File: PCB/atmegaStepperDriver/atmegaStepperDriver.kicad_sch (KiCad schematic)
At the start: 74 parts, among them J1 General power, J2 Motor Output, J3 Motor power, J4 Conn_01x05_Socket, J5 Reset Header, J6 I2C Communication pins, J9 Stepper communication pins, Q1 TIP42C, Q10 BC547, Q11 BC557, Q12 BC547, Q13 BC557, Q14 BC547, Q15 BC557, Q16 BC547, Q2 TIP41C, Q3 TIP42C, Q4 TIP42C, Q5 TIP42C, Q6 TIP41C, Q7 TIP41C, Q8 TIP41C, Q9 BC557, U1 ATmega328P-P, U2 LM7805_TO220, Y1 Crystal

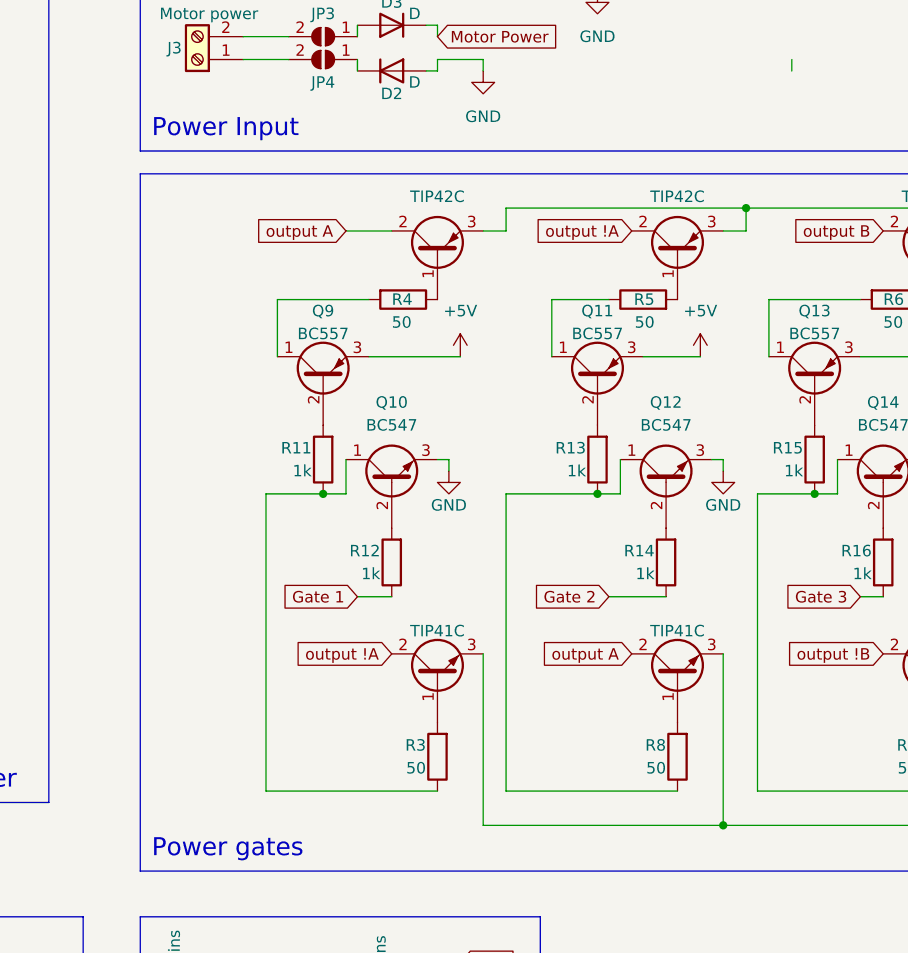
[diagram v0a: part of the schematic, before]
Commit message: new design; the old one doesn't work; to be finished;
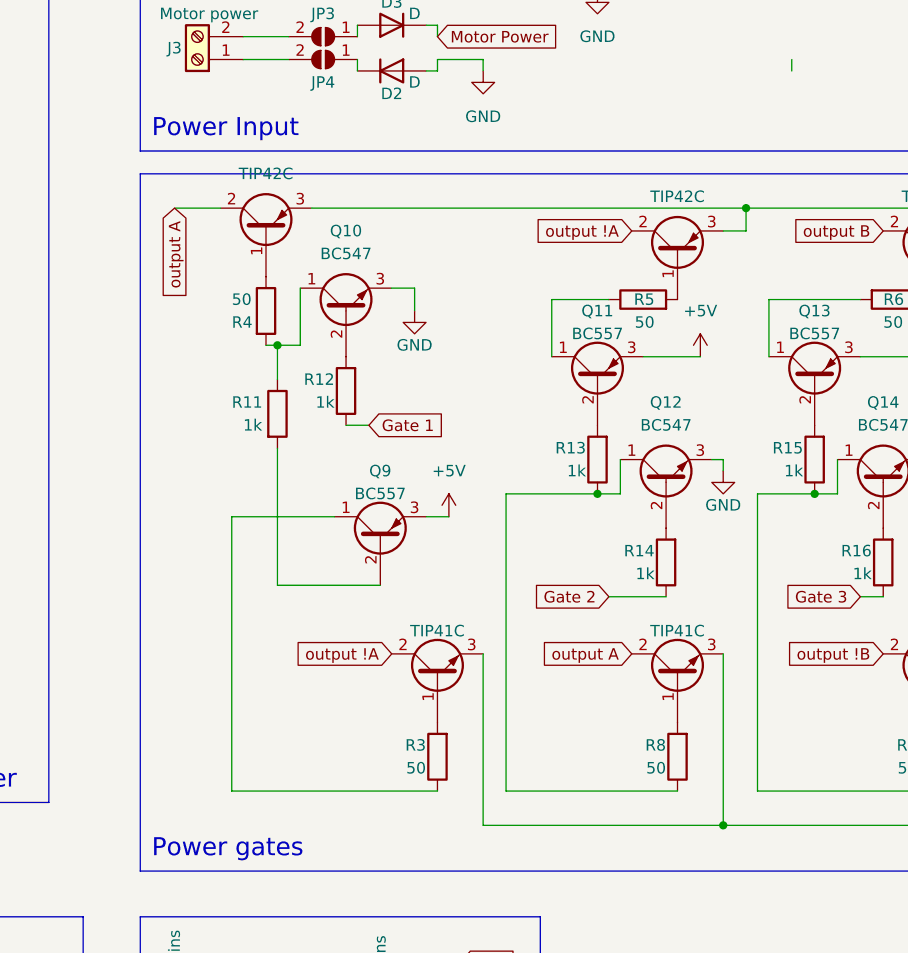
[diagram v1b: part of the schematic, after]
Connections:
- net at Q10.1 (C), R11.1: now also R4.2; no longer R3.1
- net at Q9.1 (C): now also R3.1; no longer R4.2
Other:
- moved on the sheet: Q10, Q9, R11, R12, R4

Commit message: fixed old design flaw; full redisgn; Few things to be done; V0.8.0;
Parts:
- removed J4: Conn_01x05_Socket, Connector_PinHeader_2.54mm:PinHeader_1x05_P2.54mm_Vertical, symbol Connector:Conn_01x05_Socket
- removed Q12, Q16: BC547, Package_TO_SOT_THT:TO-92_Inline, symbol Transistor_BJT:BC547
- removed Q13: BC557, Package_TO_SOT_THT:TO-92_Inline, symbol Transistor_BJT:BC557
- removed Q5: TIP42C, Package_TO_SOT_THT:TO-220-3_Vertical, symbol Transistor_BJT:TIP42C
- removed Q6, Q7: TIP41C, Package_TO_SOT_THT:TO-220-3_Vertical, symbol Transistor_BJT:TIP41C
- added D7: LED, LED_THT:LED_D5.0mm, symbol Device:LED
- added J8: Conn_01x06_Socket, Connector_PinHeader_2.54mm:PinHeader_1x06_P2.54mm_Vertical, symbol Connector:Conn_01x06_Socket
- added Q12, Q16: TIP41C, Package_TO_SOT_THT:TO-220-3_Vertical, symbol Transistor_BJT:TIP41C
- added Q13: TIP42C, Package_TO_SOT_THT:TO-220-3_Vertical, symbol Transistor_BJT:TIP42C
- added Q5, Q6: BC547, Package_TO_SOT_THT:TO-92_Inline, symbol Transistor_BJT:BC547
- added Q7: BC557, Package_TO_SOT_THT:TO-92_Inline, symbol Transistor_BJT:BC557
- added R19: 220, Resistor_THT:R_Axial_DIN0207_L6.3mm_D2.5mm_P10.16mm_Horizontal, symbol Device:R
- R14, R15, R18: value 1k -> 50
- R7, R8, R9: value 50 -> 1k
- U2: footprint Package_TO_SOT_THT:TO-220-3_Horizontal_TabDown -> Package_TO_SOT_THT:TO-220-3_Vertical
- renumbered C8 to C2-1, C9 to C2-2, C10 to C2-3, C11 to C2-4, JP5 to JP1, JP6 to JP2, JP7 to JP3, JP8 to JP4, JP3 to JP5, JP4 to JP6, JP2 to JP7
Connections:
- net +5V: now also J8.3 (Pin_3), Q7.3 (E)
- net DTR: now also J8.6 (Pin_6)
- net GND: now also D7.1 (K), J8.1 (Pin_1), Q12.3 (E), Q16.3 (E), Q5.3 (E), Q6.3 (E)
- net Gate 2: now also R13.1; no longer R14.1
- net Gate 3: now also R9.1; no longer R16.1
- net Gate 4: now also R17.1; no longer R18.1
- net Motor Power: now also Q13.3 (E)
- net output !B: now also Q8.2 (C), Q13.2 (C)
- net output A: now also Q12.2 (C)
- net output B: now also Q16.2 (C); no longer Q8.2 (C)
- net at R6.2: now also R7.1, Q5.1 (C)
- net at R15.2: now also Q14.1 (C), R16.1
- net at R5.1: now also Q3.1 (B); no longer Q11.1 (C)
- net at R5.2: now also R8.1, Q6.1 (C); no longer Q3.1 (B)
- net at R9.2: now also Q5.2 (B)
- net at Q14.2 (B): now also R17.2; no longer R16.2
- net at R10.1: now also Q7.1 (C); no longer R17.1
- net at Q15.2 (B): now also R16.2; no longer R17.2
- net at Q15.1 (C): now also R18.1; no longer R7.1
- net at R7.2: now also Q7.2 (B)
- net at R18.2: now also Q16.1 (B)
- net at R14.2: now also Q12.1 (B)
- net at R8.2: now also Q11.2 (B)
- net at R13.2: now also Q6.2 (B); no longer Q11.2 (B)
- net at U1.11 (PD5): now also R19.1
- net RX renamed TXD
- net TXD: now also J8.5 (Pin_5)
- net TX renamed RXD
- net RXD: now also J8.4 (Pin_4)
- new net: D7.2 (A), R19.2
- new net: Q11.1 (C), R14.1
- new net: Q13.1 (B), R15.1

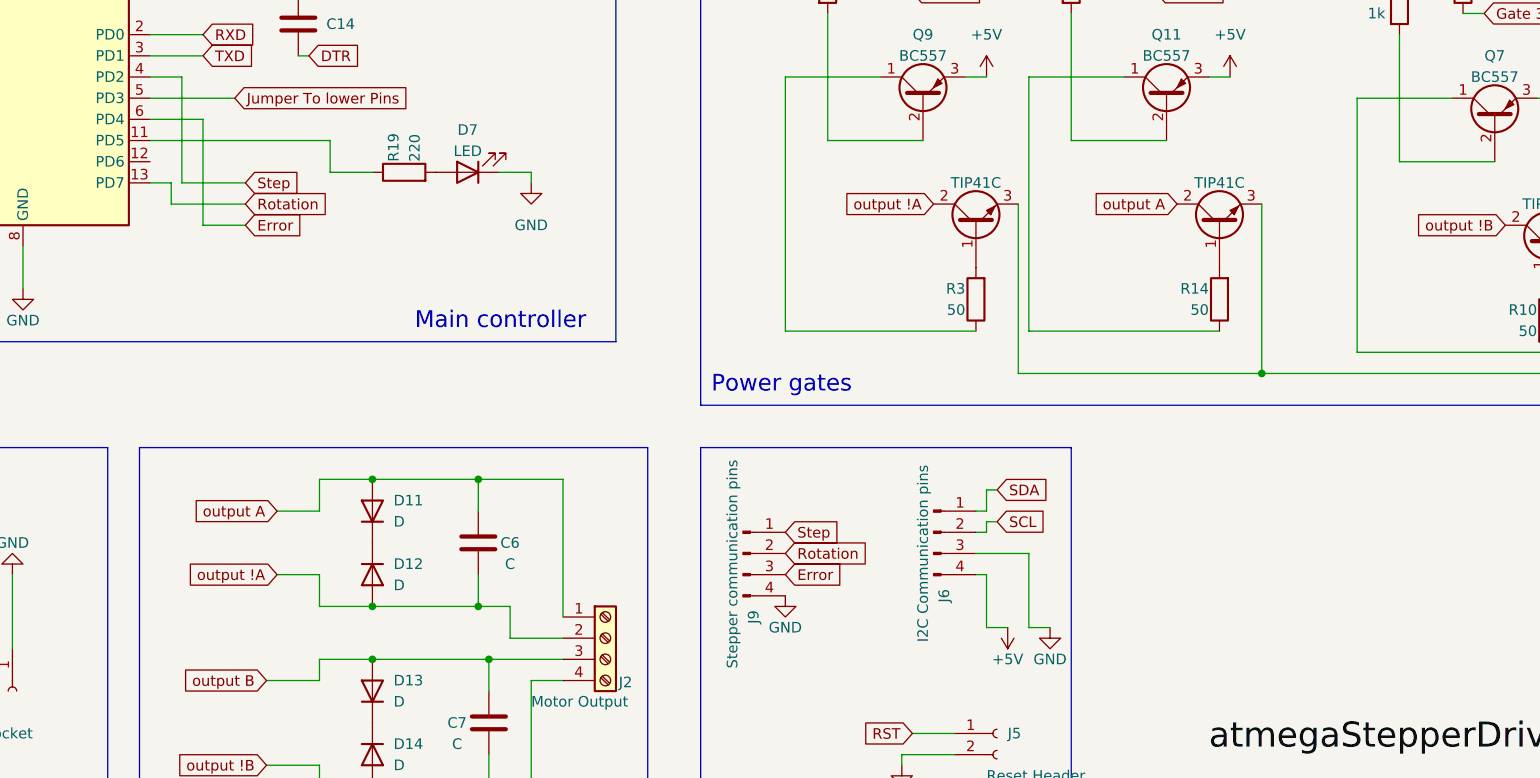
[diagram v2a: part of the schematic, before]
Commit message: traces fixed; fan added; V0.8.1
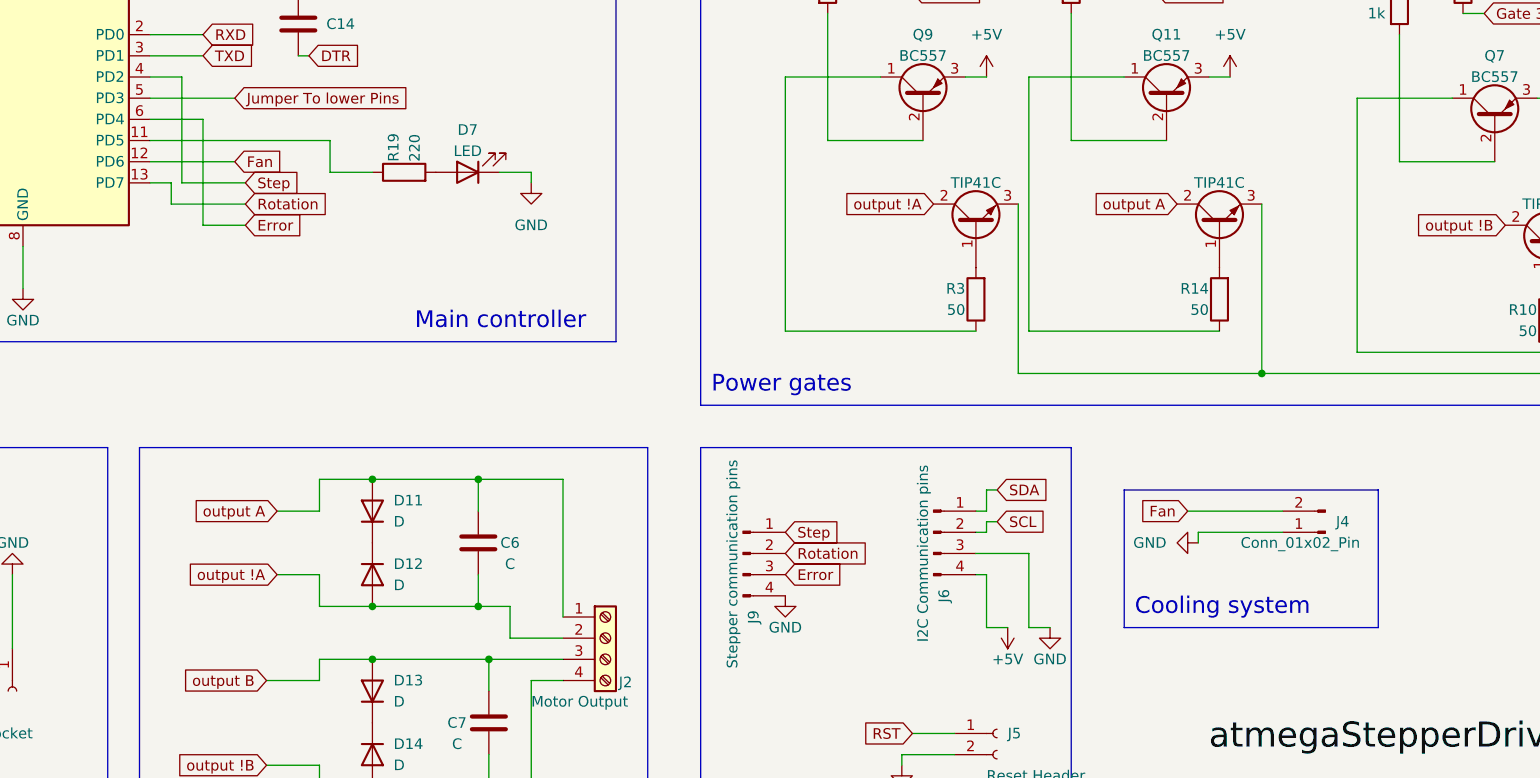
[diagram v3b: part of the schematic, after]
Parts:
- added J4: Conn_01x02_Pin, Connector_PinHeader_2.54mm:PinHeader_1x02_P2.54mm_Vertical, symbol Connector:Conn_01x02_Pin
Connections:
- net GND: now also J4.1 (Pin_1)
- net Fan: now reaches U1.12 (PD6)
- net Fan: now also J4.2 (Pin_2)
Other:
- note added: "Cooling system"
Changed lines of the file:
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@@
   (title_block
     (title "atmegaStepperDriver Developer board")
-    (date "2023-08-29")
-    (rev "V0.8.0")
+    (date "2023-08-30")
+    (rev "V0.8.1")
   )
   (junction (at 187.96 130.81) (diameter 0) (color 0 0 0 0)
@@
     (stroke (width 0) (type default))
   )
+  (wire (pts (xy 180.34 149.86) (xy 190.5 149.86))
+    (stroke (width 0) (type default))
+  )
   (wire (pts (xy 151.13 69.85) (xy 151.13 72.39))
     (stroke (width 0) (type default))
@@
     (stroke (width 0) (type default))
   )
+  (wire (pts (xy 180.34 149.86) (xy 180.34 151.13))
+    (stroke (width 0) (type default))
+  )
   (wire (pts (xy 57.15 107.95) (xy 57.15 110.49))
     (stroke (width 0) (type default))
@@
     (stroke (width 0) (type default))
   )
+  (wire (pts (xy 54.61 105.41) (xy 64.77 105.41))
+    (stroke (width 0) (type default))
+  )
   (wire (pts (xy 207.01 72.39) (xy 207.01 78.74))
     (stroke (width 0) (type default))
@@
     (stroke (width 0) (type default))
   )
+  (wire (pts (xy 179.07 147.32) (xy 190.5 147.32))
+    (stroke (width 0) (type default))
+  )
   (wire (pts (xy 144.78 27.94) (xy 144.78 26.67))
     (stroke (width 0) (type default))
@@
     (fill (type none))
   )
+  (rectangle (start 171.45 144.78) (end 201.93 161.29)
+    (stroke (width 0) (type default))
+    (fill (type none))
+  )
   (rectangle (start 120.65 57.15) (end 274.32 134.62)
     (stroke (width 0) (type default))
@@
     (effects (font (size 2 2)) (justify left bottom))
   )
+  (text "Cooling system\n" (at 172.72 160.02 0)
+    (effects (font (size 2 2)) (justify left bottom))
+  )
   (text "Power Output\n" (at 54.61 185.42 0)
     (effects (font (size 2 2)) (justify left bottom))
@@
     )
   )
+  (global_label "Fan" (shape input) (at 179.07 147.32 180) (fields_autoplaced)
+    (effects (font (size 1.27 1.27)) (justify right))
+    (property "Intersheetrefs" "${INTERSHEET_REFS}" (at 172.6982 147.32 0)
+      (effects (font (size 1.27 1.27)) (justify right) hide)
+    )
+  )
   (global_label "output !B" (shape input) (at 217.17 113.03 180) (fields_autoplaced)
     (effects (font (size 1.27 1.27)) (justify right))
@@
     )
   )
+  (global_label "Fan" (shape input) (at 64.77 105.41 0) (fields_autoplaced)
+    (effects (font (size 1.27 1.27)) (justify left))
+    (property "Intersheetrefs" "${INTERSHEET_REFS}" (at 71.1418 105.41 0)
+      (effects (font (size 1.27 1.27)) (justify left) hide)
+    )
+  )
   (symbol (lib_id "Jumper:SolderJumper_2_Open") (at 140.97 44.45 180) (unit 1)
     (in_bom yes) (on_board yes) (dnp no)
@@
     )
   )
+  (symbol (lib_id "power:GND") (at 180.34 151.13 270) (unit 1)
+    (in_bom yes) (on_board yes) (dnp no) (fields_autoplaced)
+    (property "Reference" "#PWR029" (at 173.99 151.13 0)
+      (effects (font (size 1.27 1.27)) hide)
+    )
+    (property "Value" "GND" (at 176.53 151.13 90)
+      (effects (font (size 1.27 1.27)) (justify right))
+    )
+    (property "Footprint" "" (at 180.34 151.13 0)
+      (effects (font (size 1.27 1.27)) hide)
+    )
+    (property "Datasheet" "" (at 180.34 151.13 0)
+      (effects (font (size 1.27 1.27)) hide)
+    )
+    (pin "1")
+    (instances
+      (project "atmegaStepperDriver"
+        (path "/c84e7e69-c1fd-4499-93bc-6ad0c4ebade1"
+          (reference "#PWR029") (unit 1)
+        )
+      )
+    )
+  )
   (symbol (lib_id "Regulator_Linear:LM7805_TO220") (at 232.41 29.21 0) (unit 1)
     (in_bom yes) (on_board yes) (dnp no) (fields_autoplaced)
@@
         )
       )
+    )
+  )
+  (symbol (lib_id "Connector:Conn_01x02_Pin") (at 195.58 149.86 180) (unit 1)
+    (in_bom yes) (on_board yes) (dnp no)
+    (property "Reference" "J4" (at 196.85 148.59 0)
+      (effects (font (size 1.27 1.27)) (justify right))
+    )
+    (property "Value" "Conn_01x02_Pin" (at 185.42 151.13 0)
+      (effects (font (size 1.27 1.27)) (justify right))
+    )
+    (property "Footprint" "Connector_PinHeader_2.54mm:PinHeader_1x02_P2.54mm_Vertical" (at 195.58 149.86 0)
+      (effects (font (size 1.27 1.27)) hide)
+    )
+    (property "Datasheet" "~" (at 195.58 149.86 0)
+      (effects (font (size 1.27 1.27)) hide)
+    )
+    (pin "1")
+    (pin "2")
+    (instances
+      (project "atmegaStepperDriver"
+        (path "/c84e7e69-c1fd-4499-93bc-6ad0c4ebade1"
+          (reference "J4") (unit 1)
+        )
+      )
